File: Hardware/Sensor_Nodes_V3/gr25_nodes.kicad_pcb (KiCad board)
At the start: 4 copper layers, 22.4 x 70.5 mm, 73 parts, among them J1 Conn_01x06_Socket, J2 Conn_01x27_Socket, J3 Conn_01x27_Socket, Q1 S9013, U1 STM32F103C8Tx, U2 STM32G474RBTx, U3 MCP2542FDxMF, U4 MCP2542FDxMF, U5 AMS1117-3.3, U6 TPS563200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

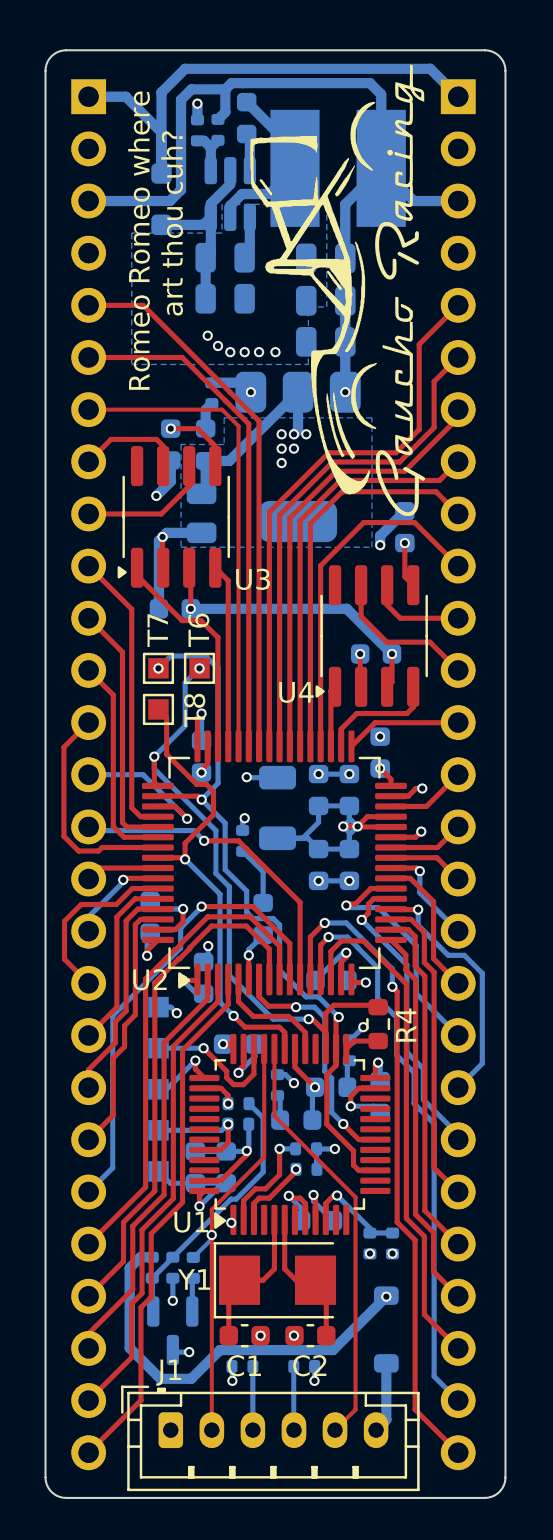
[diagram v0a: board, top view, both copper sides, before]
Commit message: fixed the CAN issue and rerouted some things. Added a solder bridge for Vref so that there is a choice of using it or not.
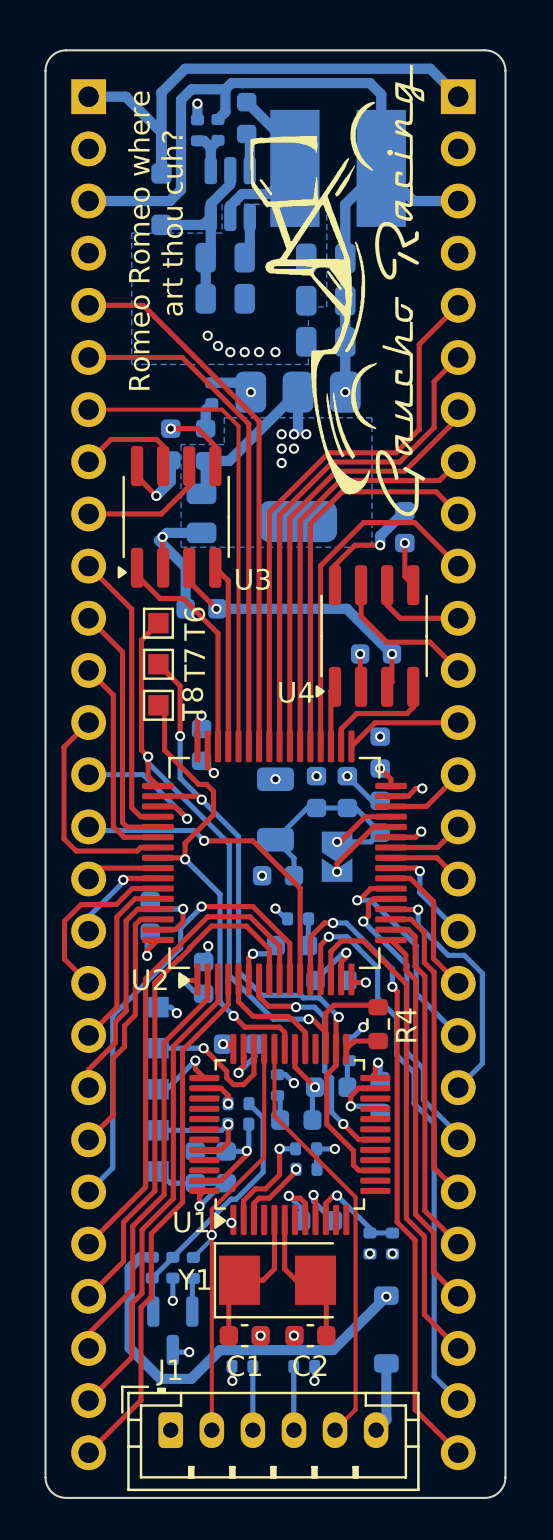
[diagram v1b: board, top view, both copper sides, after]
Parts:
- added JP1: SolderJumper_2_Open, Jumper:SolderJumper-2_P1.3mm_Open_TrianglePad1.0x1.5mm, B.Cu at (122.8, 66.8)
- moved R15 4.66 mm to (120.9, 69.8), turned to 0 degrees
- moved C12 4.62 mm to (119.9, 67.7), turned to 180 degrees
- moved C19 3.55 mm to (121.8, 63.6), turned to 90 degrees
- moved T6 2.97 mm to (114.1, 55.4)
- moved C16 2.79 mm to (124.9, 64.8), turned to 90 degrees
- moved D4 1.91 mm to (120.6, 71.1), turned to 180 degrees
- moved C20 1.30 mm to (116.2, 54.7)
- moved C10 0.57 mm to (116.2, 61.3)
- moved T7 0.20 mm to (114.1, 57.4)
- moved T8 0.20 mm to (114.1, 59.4)
- moved C9 0.14 mm to (123.3, 63.6)
- moved L1 0.13 mm to (119.8, 64.5)
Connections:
- U2 pad 28: VDDA -> Net-(JP1-B)
- U3 pad 8: unconnected-(U3-STBY-Pad8) -> GND
- U4 pad 8: unconnected-(U4-STBY-Pad8) -> GND
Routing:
- net GND: track 56.7 -> 62.8 mm, vias 37 -> 36
- net Net-(JP1-B): track 0.00 -> 3.77 mm, vias 0 -> 1
- net VDDA: track 17.3 -> 13.8 mm, vias 2 -> 1
- net +3.3V: track 41.5 -> 39.2 mm
- net T_CLK: track 35.8 -> 33.7 mm
- net T_DIO: track 30.3 -> 32.3 mm, vias 3 -> 2
- net Net-(D4-K): track 2.93 -> 1.30 mm
- net PC4: track 12.0 -> 10.9 mm
- net D-: track 21.4 -> 20.6 mm
- net +5V: track 123.4 -> 122.7 mm
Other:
- board text added: "@an0tv 1/13/25"
- board text added: "V3.1"
- board text removed: "@an0tv 10/2/24"

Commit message: redud some of the zones and changed the thermal relief to not be traces but filled zones
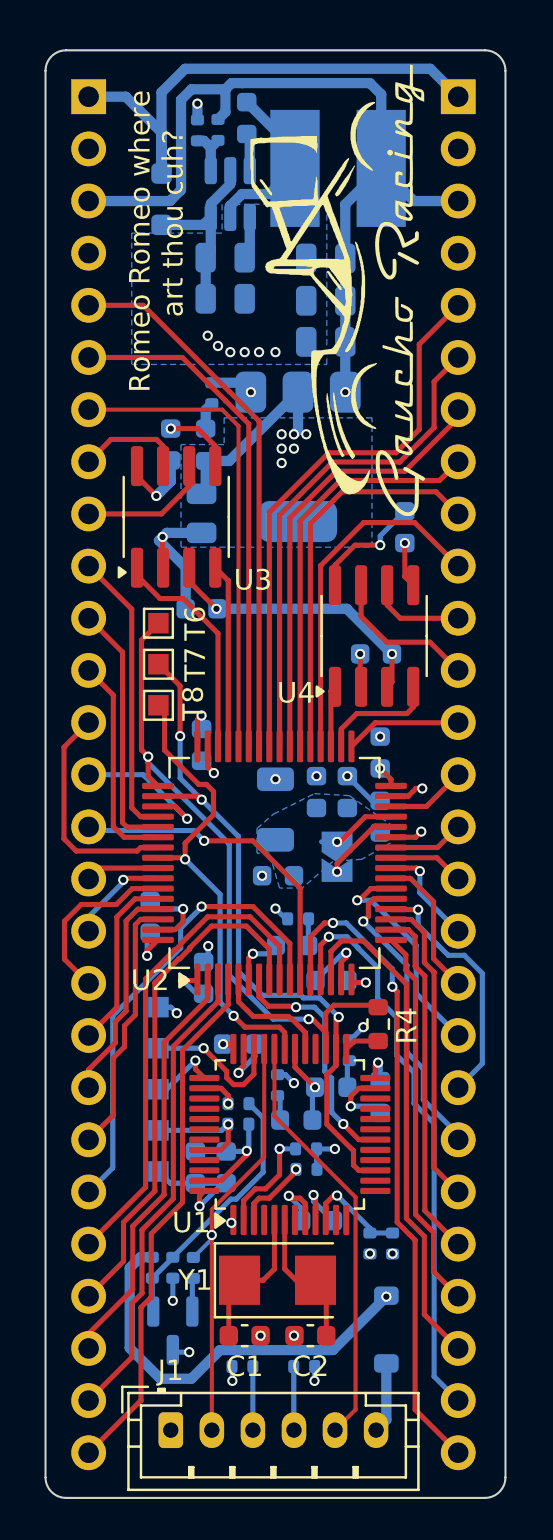
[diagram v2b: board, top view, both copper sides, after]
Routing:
- net VDDA: track 13.8 -> 3.89 mm
- added copper zone on B.Cu, net VDDA
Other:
- board text added: "@an0tv 1/14/25"
- board text removed: "@an0tv 1/13/25"

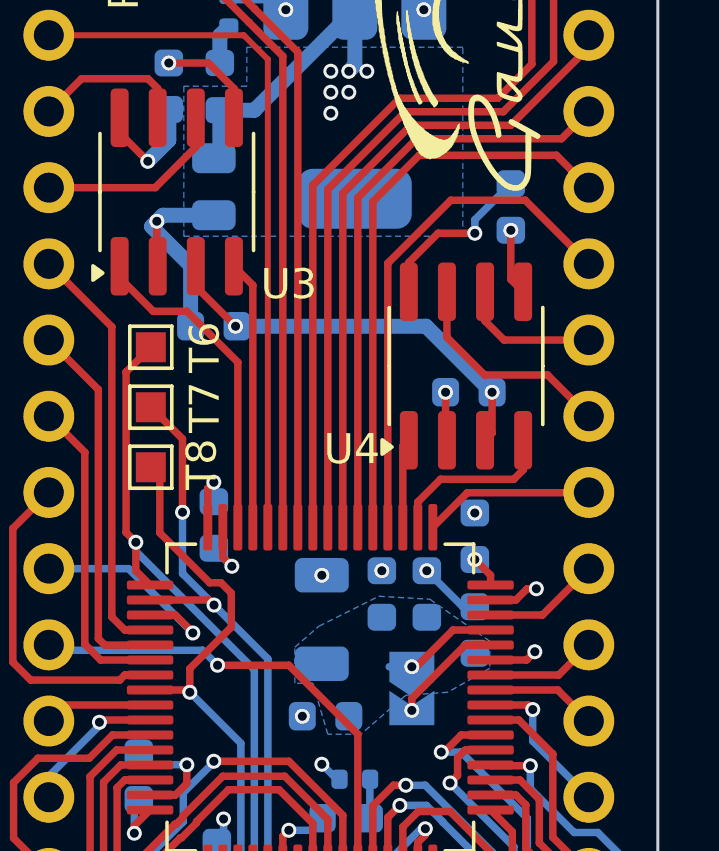
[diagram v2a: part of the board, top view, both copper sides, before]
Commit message: redid two traces, changed data
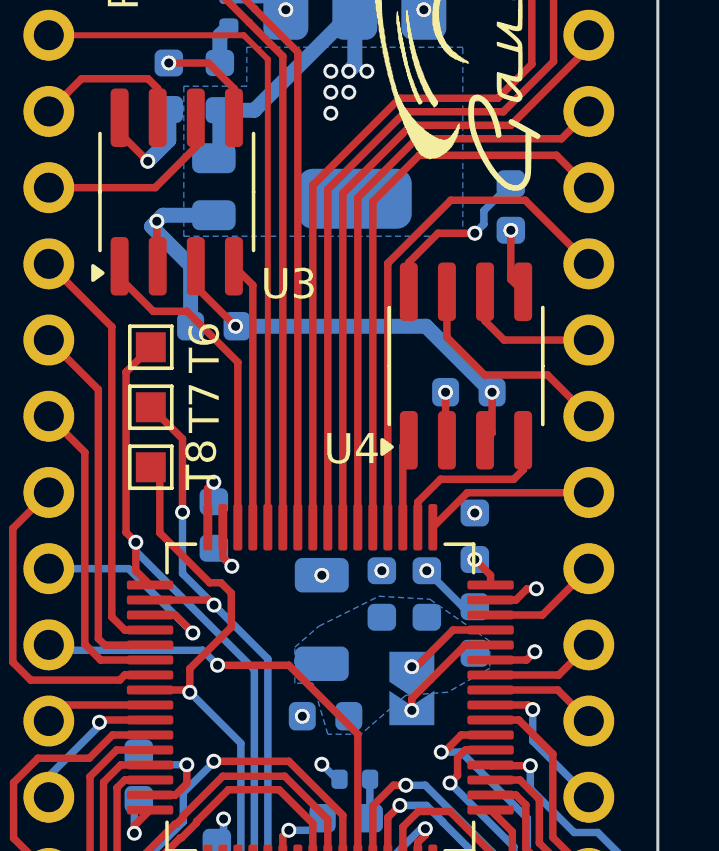
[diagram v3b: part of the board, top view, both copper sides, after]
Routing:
- net VDDA: track 3.89 -> 3.13 mm
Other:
- board text added: "@an0tv 1/30/25"
- board text removed: "@an0tv 1/14/25"

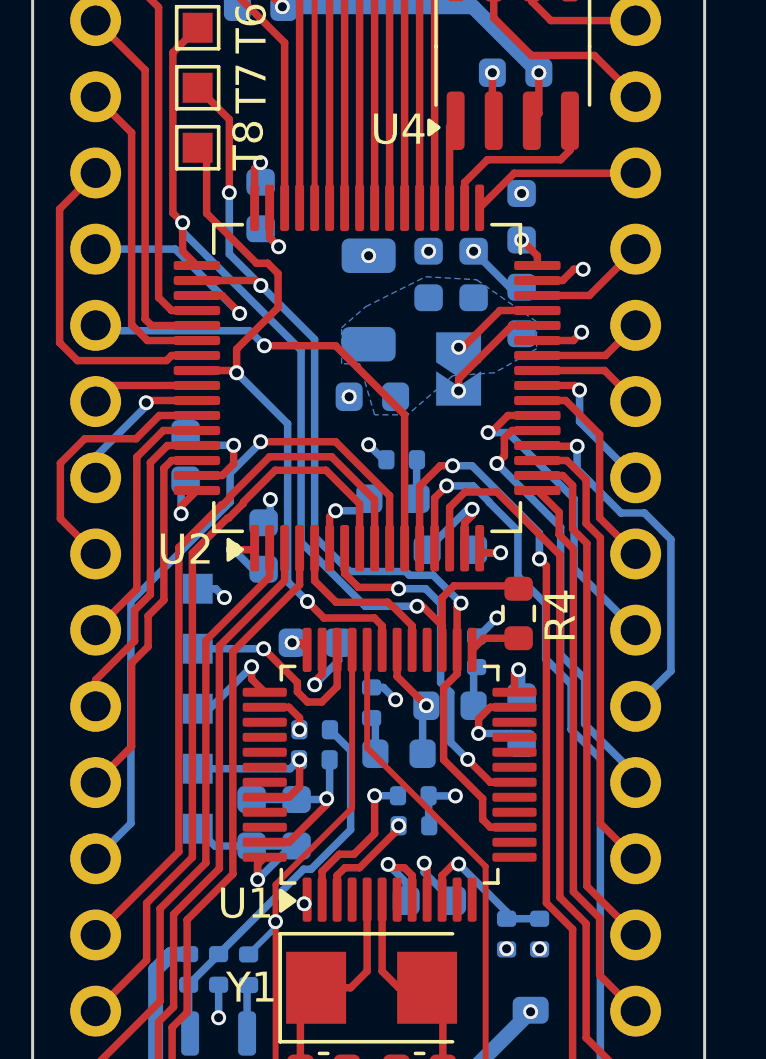
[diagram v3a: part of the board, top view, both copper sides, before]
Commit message: V3.2 SAM Board added, CHASSES TOF code added and some TCM-CAN stuff added
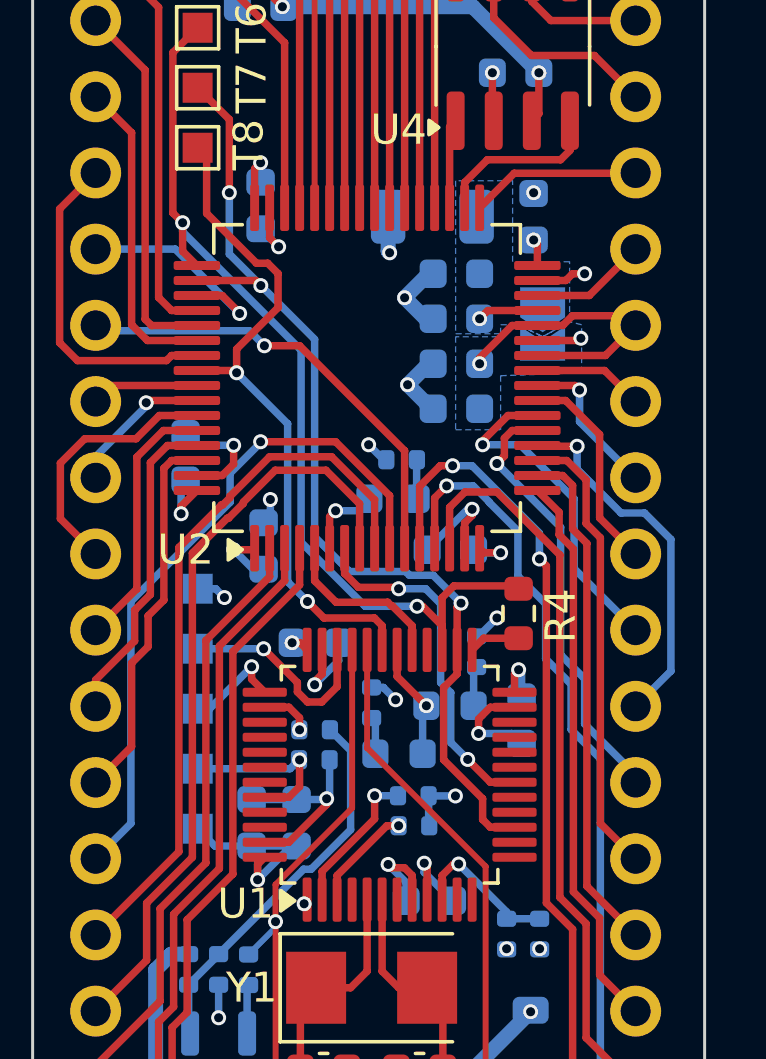
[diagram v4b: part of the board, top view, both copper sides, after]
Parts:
- moved C19 4.57 mm to (122.7, 68.1), turned to 180 degrees
- moved C12 3.82 mm to (122.7, 65.1)
- moved L1 3.50 mm to (121.9, 61.7), turned to 0 degrees
- moved JP1 3.18 mm to (125.6, 65.3)
- moved C16 2.81 mm to (122.7, 66.6), turned to 180 degrees
- moved C9 0.58 mm to (122.7, 63.6), turned to 180 degrees
- moved C15 0.40 mm to (125.3, 61.7)
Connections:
- C16 pad 1: VDDA -> PB2/VREF
- C19 pad 1: VDDA -> PB2/VREF
- J2 pad 15: PB2 -> PB2/VREF
- JP1 pad 2: Net-(JP1-B) -> PB2/VREF
- U2 pad 26: PB2 -> PB2/VREF
- U2 pad 28: Net-(JP1-B) -> PB2/VREF
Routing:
- net PB2/VREF: track 0.00 -> 9.80 mm, vias 0 -> 1
- net Net-(JP1-B): track 3.77 -> 0.00 mm, vias 1 -> 0
- net PB2: track 3.69 -> 0.00 mm
- net GND: track 62.8 -> 65.5 mm, vias 36 -> 35
- net +3.3V: track 39.2 -> 40.3 mm
- net VDDA: track 3.13 -> 2.18 mm
- net PC3: track 16.0 -> 15.3 mm
- added copper zone on B.Cu, net PB2/VREF
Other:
- board text added: "V3.2"
- board text removed: "V3.1"

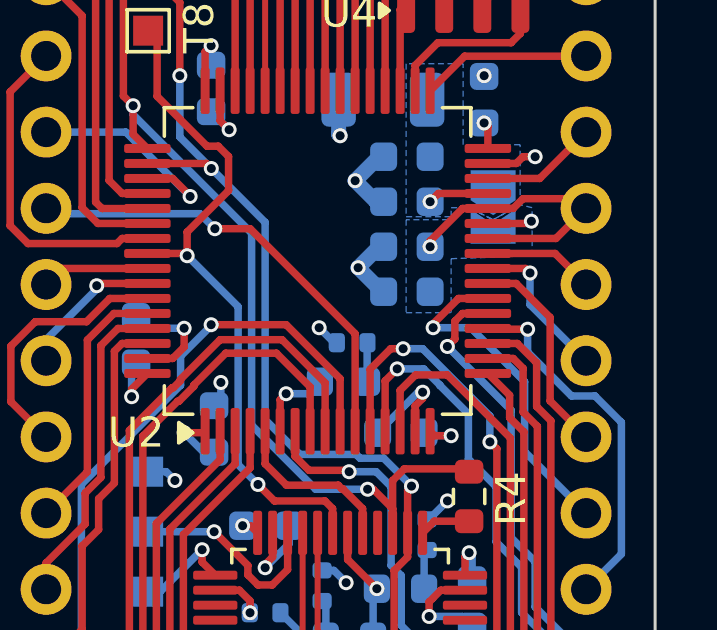
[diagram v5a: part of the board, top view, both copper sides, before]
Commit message: fixed pin names
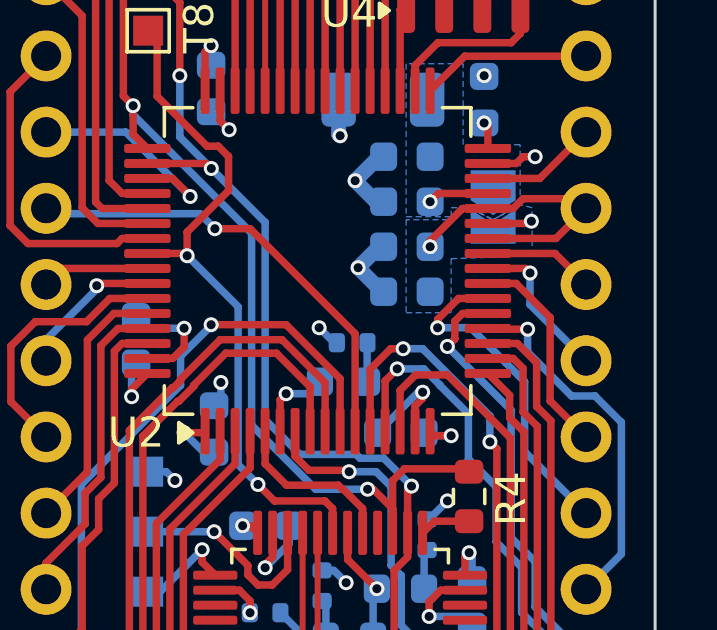
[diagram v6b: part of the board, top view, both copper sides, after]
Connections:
- net CANH3 renamed CANH1
- net CANL3 renamed CANL1
- net CRXD3 renamed CRXD1
- net CTXD3 renamed CTXD1
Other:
- board text added: "V3.3"
- board text removed: "V3.2"

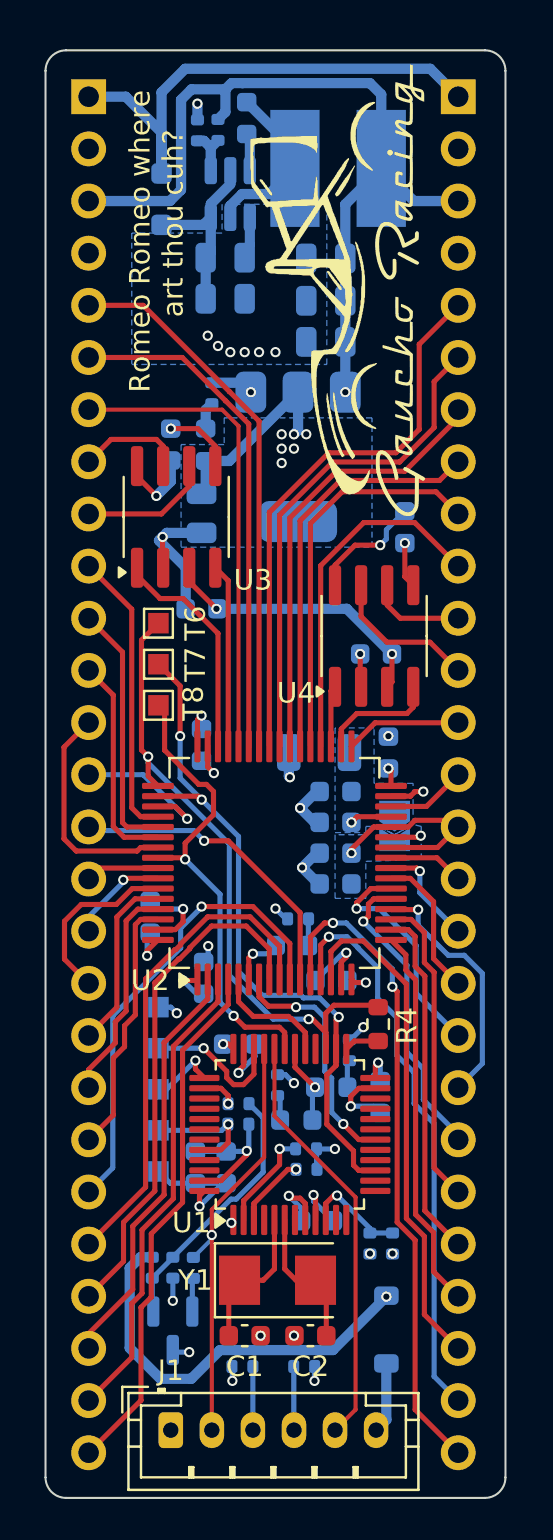
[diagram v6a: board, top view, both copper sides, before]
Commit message: added pin numbers
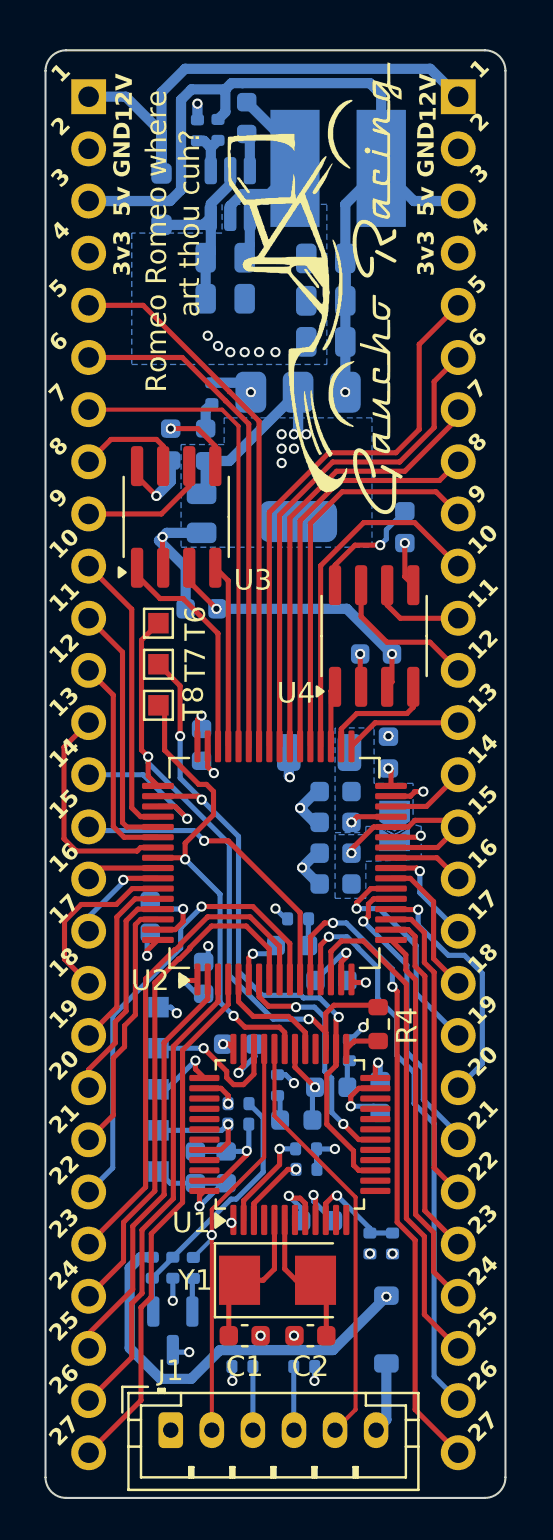
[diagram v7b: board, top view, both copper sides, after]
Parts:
- moved G*** 1.10 mm to (121.7, 39.1)
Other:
- board text added: "1"
- board text added: "10"
- board text added: "11"
- board text added: "12"
- board text added: "12V"
- board text added: "13"
- board text added: "14"
- board text added: "15"
- board text added: "16"
- board text added: "17"
- board text added: "18"
- board text added: "19"
- board text added: "2"
- board text added: "20"
- board text added: "21"
- board text added: "22"
- board text added: "23"
- board text added: "24"
- board text added: "25"
- board text added: "26"
- board text added: "27"
- board text added: "3"
- board text added: "3v3"
- board text added: "4"
- board text added: "5"
- board text added: "5v"
- board text added: "6"
- board text added: "7"
- board text added: "8"
- board text added: "9"
- board text added: "GND"
